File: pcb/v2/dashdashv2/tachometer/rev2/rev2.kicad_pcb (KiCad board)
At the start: 4 copper layers, 95 x 77 mm, 204 parts, among them J1 Tag connect, J2 RPM_CONN1, Q1 BSS138, Q2 BSS138, Q6 BSS138, Q7 BSS138, U1 W25Q128JVS, U2 LP5907MFX-3.3, U3 SRV05-4, U4 RP2040, U6 YAAJ_DCDC_StepDown_LM2596, Y1 12MHz

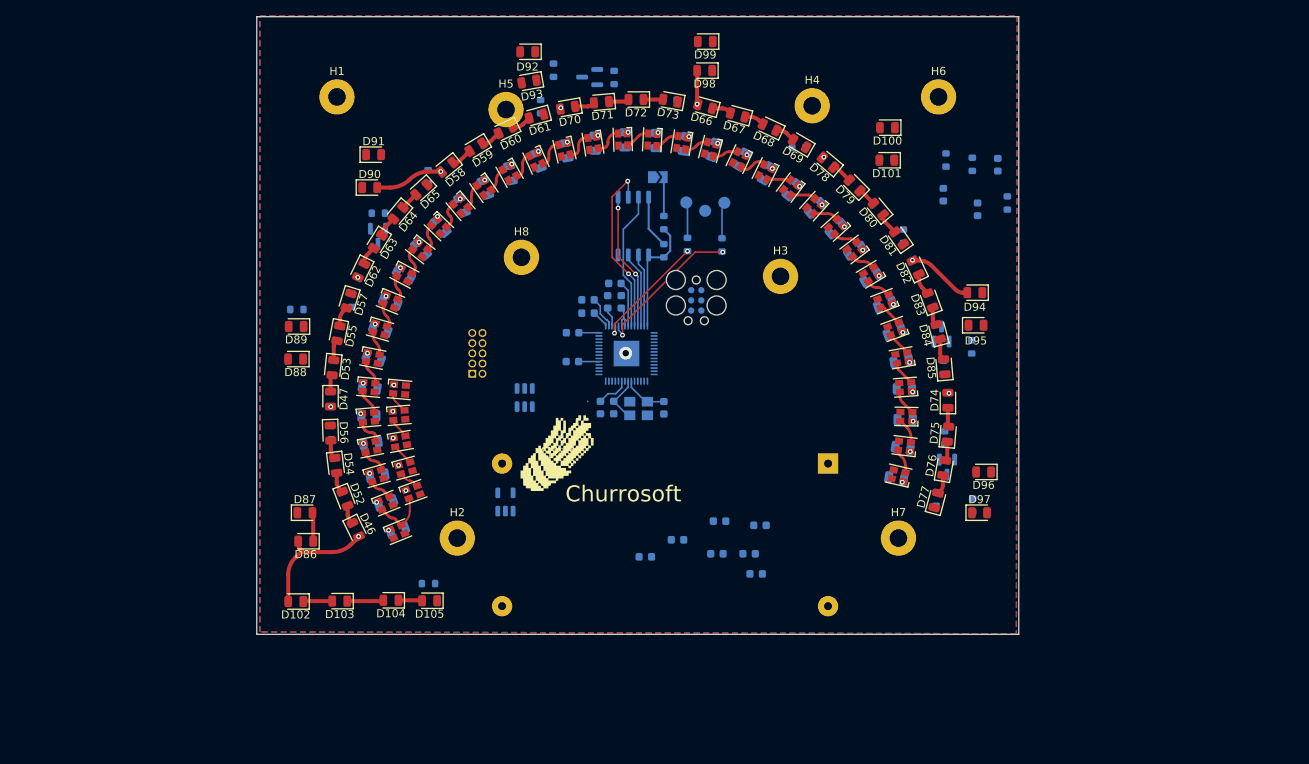
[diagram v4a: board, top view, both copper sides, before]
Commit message: routing backlight leds
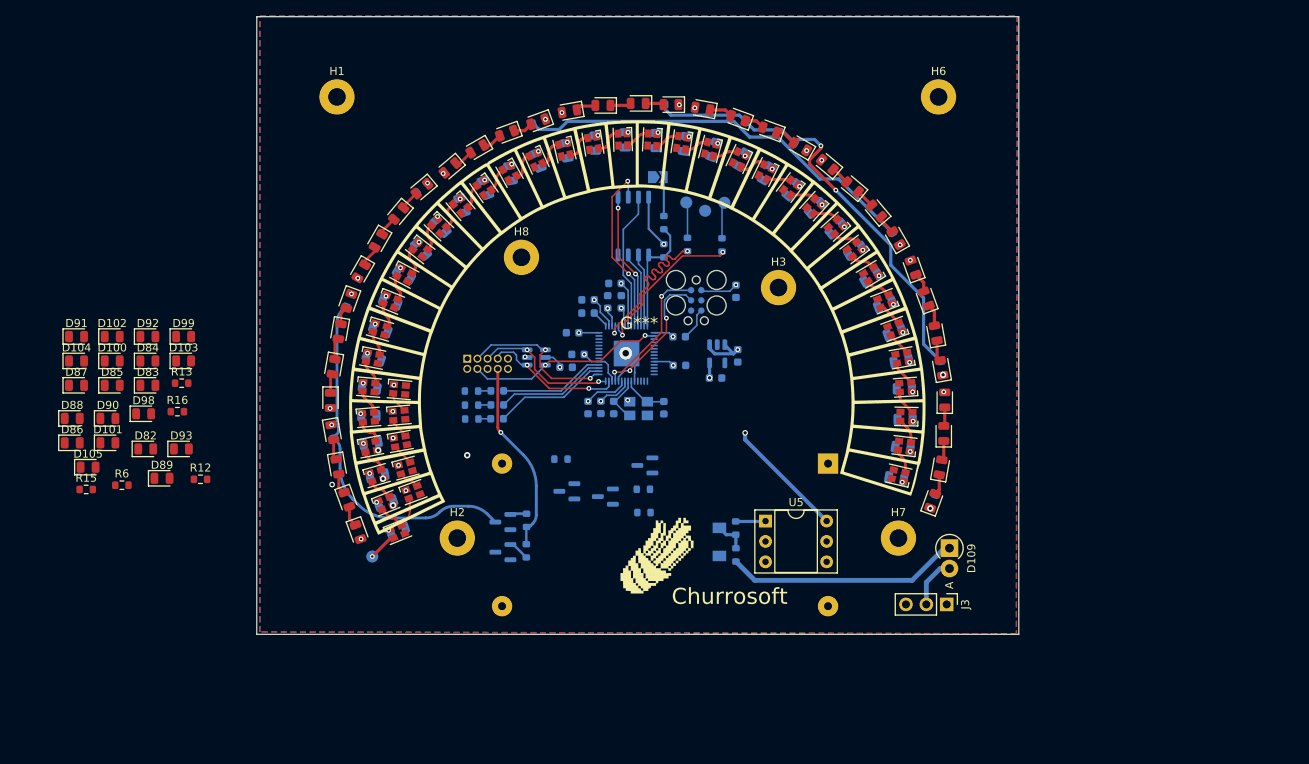
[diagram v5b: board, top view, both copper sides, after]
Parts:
- removed H5: MountingHole, MountingHole:MountingHole_2.2mm_M2_Pad
- removed R17, R19, R20: 1k 1/10W +-1%, Resistor_SMD:R_0603_1608Metric
- added D109: 1N4007, Diode_THT:D_DO-41_SOD81_P2.54mm_Vertical_AnodeUp, F.Cu at (186.4, 116.3)
- added D110: BZV55B5V1, Diode_SMD:D_MiniMELF, B.Cu at (157.7, 115.5)
- added G***: LOGO, LOGO, F.Cu at (147.7, 88.2)
- added J3: Conn_01x03, Connector_PinHeader_2.54mm:PinHeader_1x03_P2.54mm_Vertical, F.Cu at (186.0, 123.3)
- added Q8: BSS138, Package_TO_SOT_SMD:SOT-23, B.Cu at (148.4, 105.9)
- added R12: 1k 1/10W +-1%, Resistor_SMD:R_0603_1608Metric, F.Cu at (93.0, 107.7)
- added R13: 1k 1/10W +-1%, Resistor_SMD:R_0603_1608Metric, F.Cu at (90.6, 95.7)
- added R2: 1k 1/10W +-1%, Resistor_SMD:R_0603_1608Metric, B.Cu at (148.2, 108.9)
- added R36: 1k 1/10W +-1%, Resistor_SMD:R_0603_1608Metric, B.Cu at (159.7, 117.1)
- added R37: 330R 1/10W +-1%, Resistor_SMD:R_0603_1608Metric, B.Cu at (159.7, 113.8)
- added R6: 1k 1/10W +-1%, Resistor_SMD:R_0603_1608Metric, F.Cu at (83.2, 108.4)
- added U5: H11L1, Package_DIP:DIP-6_W7.62mm_Socket, F.Cu at (163.4, 112.9)
- H4: value MountingHole -> USB_GND; footprint MountingHole:MountingHole_2.2mm_M2_Pad -> TestPoint:TestPoint_Pad_D1.5mm; moved to B.Cu
- R15, R16: moved to F.Cu
- moved R15 108.0 mm to (78.7, 108.9), turned to 0 degrees
- moved D85 103.8 mm to (82.0, 96.0), turned to 0 degrees
- moved D101 103.3 mm to (81.4, 103.1), turned to 0 degrees
- moved D100 100.9 mm to (82.0, 92.9), turned to 0 degrees
- moved D82 98.6 mm to (86.2, 103.9), turned to 0 degrees
- moved D84 98.6 mm to (86.4, 92.9), turned to 0 degrees
- moved D83 98.1 mm to (86.4, 96.0), turned to 0 degrees
- moved D98 82.0 mm to (85.9, 99.5), turned to 0 degrees
- moved H4 78.5 mm to (114.4, 117.3), turned to 180 degrees
- moved R28 74.8 mm to (184.3, 110.4), turned to 70 degrees
- moved D99 74.7 mm to (90.9, 89.9), turned to 0 degrees
- moved D64 74.7 mm to (185.2, 106.2), turned to 80 degrees
- moved D65 74.6 mm to (184.3, 110.3), turned to 70 degrees
- moved D62 74.5 mm to (185.8, 97.8), turned to 90 degrees
- moved D63 74.5 mm to (185.6, 102.0), turned to 90 degrees
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- renumbered G*** to Churrosoft
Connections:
- H4 pad 1: (no net) -> /TACH_DIN
- R15 pad 1: Net-(D85-Pad1) -> Net-(D101-Pad1)
- R15 pad 2: /BA_3 -> /BA_5
- R16 pad 1: Net-(D89-Pad1) -> Net-(D105-Pad1)
- R16 pad 2: /BA_3 -> /BA_5
- U3 pad 1: CLK -> MOSI
- U3 pad 4: RPM_CS -> CLK
- U3 pad 6: MOSI -> RPM_CS
- U4 pad 27: CLK -> MOSI
- U4 pad 29: MOSI -> CLK
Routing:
- net +12LF: track 37.6 -> 108.9 mm, vias 9 -> 11
- net /BA_4: track 0.00 -> 56.6 mm, vias 0 -> 2
- net /BA_3: track 0.00 -> 51.4 mm
- net /BA_1: track 0.00 -> 44.6 mm
- net +3V3: track 19.2 -> 56.3 mm, vias 0 -> 12
- net Net-(D109-Pad1): track 0.00 -> 29.3 mm
- net RPM_CS: track 0.00 -> 24.8 mm, vias 0 -> 2
- net PWM_BACK_RPM: track 0.00 -> 24.2 mm, vias 0 -> 1
- net CLK: track 0.00 -> 20.0 mm, vias 0 -> 2
- net MISO: track 0.00 -> 18.0 mm, vias 0 -> 2
- net +1V1: track 12.5 -> 30.5 mm, vias 0 -> 3
- net /SYS_SWDIO: track 0.00 -> 17.6 mm, vias 0 -> 2
- net MOSI: track 0.00 -> 17.5 mm, vias 0 -> 2
- net /SYS_SWCLK: track 0.00 -> 16.9 mm, vias 0 -> 2
- net /LED_GREEN: track 0.00 -> 14.4 mm
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- added copper zone on In2.Cu, net +3V3
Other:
- board text removed: "Churrosoft"

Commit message: rpm routing v01
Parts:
- removed D102, D103, D104, D105: LED, LED_SMD:LED_0805_2012Metric
- removed R16: 1k 1/10W +-1%, Resistor_SMD:R_0603_1608Metric
- R12, R13, R15, R6: moved to B.Cu
- moved R15 111.0 mm to (189.7, 111.5)
- moved D100 109.9 mm to (191.0, 107.3)
- moved D101 108.7 mm to (189.8, 111.5)
- moved D98 104.8 mm to (189.7, 85.1)
- moved D99 98.9 mm to (189.8, 88.3)
- moved D92 96.0 mm to (178.7, 63.4)
- moved D93 95.2 mm to (178.8, 68.0)
- moved R13 92.3 mm to (178.7, 67.9)
- moved D91 85.9 mm to (155.7, 54.3)
- moved D90 85.9 mm to (155.7, 57.0)
- moved D88 70.6 mm to (133.9, 58.3)
- moved D89 69.3 mm to (134.0, 55.4)
- moved R12 66.3 mm to (133.9, 55.5)
- moved D86 51.4 mm to (114.4, 67.8)
- moved D87 44.1 mm to (114.2, 71.3)
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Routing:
- net /BA_5: track 0.00 -> 202.0 mm
- net /BA_2: track 0.00 -> 111.0 mm, vias 0 -> 3
- net /BA_3: track 51.4 -> 108.4 mm, vias 0 -> 2
- net /BA_4: track 56.6 -> 111.9 mm, vias 2 -> 4
- net +12LF: track 108.9 -> 139.8 mm, vias 11 -> 10
- net Net-(D87-Pad1): track 0.00 -> 30.7 mm
- net Net-(D91-Pad1): track 0.00 -> 29.5 mm
- net +5VA: track 7.47 -> 30.7 mm
- net Net-(D100-Pad2): track 0.00 -> 20.2 mm
- net Net-(D83-Pad1): track 0.00 -> 19.9 mm
- net PWM_BACK_RPM: track 24.2 -> 32.5 mm
- net Net-(D92-Pad1): track 0.00 -> 5.42 mm
- net Net-(D100-Pad1): track 0.00 -> 4.51 mm
- net Net-(D86-Pad1): track 0.00 -> 4.22 mm
- net Net-(Q8-Pad1): track 0.00 -> 4.11 mm
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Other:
- board text added: "DashDash RPM Counter v0.1"

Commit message: update neopixel
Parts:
- D1, D10, D11, D111, D112, D113, D114, D115, D12, D13, D14, D15, D16, D17, D18, D19, D2, D20, D21, D22, D23, D24, D25, D26, D27, D28, D29, D3, D30, D31, D32, D33, D34, D35, D36, D4, D5, D6, D7, D8, D9: footprint LED_SMD:LED_Cree-PLCC4_2x2mm_CW -> dashdash_lib:LED_WS2812-2020
- moved C47 0.41 mm to (180.1, 107.4), turned to 170 degrees
- moved C40 0.41 mm to (176.9, 82.2), turned to -150 degrees
- moved D113 0.40 mm to (118.3, 102.9)
- moved D111 0.39 mm to (119.9, 109.2)
- moved C46 0.38 mm to (180.9, 103.9), turned to 170 degrees
- moved C14 0.36 mm to (114.9, 106.9), turned to 20 degrees
- moved C18 0.36 mm to (114.5, 92.2), turned to -10 degrees
- moved D112 0.36 mm to (118.9, 106.2)
- moved C35 0.35 mm to (163.9, 69.6), turned to -120 degrees
- moved C42 0.35 mm to (179.8, 89.1), turned to -160 degrees
- moved C13 0.34 mm to (115.9, 110.3), turned to 20 degrees
- moved D114 0.33 mm to (118.1, 99.8)
- moved C21 0.32 mm to (118.4, 81.8), turned to -30 degrees
- moved C43 0.32 mm to (180.6, 92.8), turned to -170 degrees
- moved C12 0.32 mm to (117.3, 114.1), turned to 20 degrees
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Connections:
- D1 pad 1: +5VA -> Net-(D1-Pad1)
- D1 pad 2: Net-(D1-Pad2) -> GND
- D1 pad 3: GND -> /TACH_DIN
- D1 pad 4: /TACH_DIN -> +5VA
- D10 pad 1: +5VA -> Net-(D10-Pad1)
- D10 pad 2: Net-(D10-Pad2) -> GND
- D10 pad 3: GND -> Net-(D10-Pad3)
- D10 pad 4: Net-(D10-Pad4) -> +5VA
- D11 pad 1: +5VA -> Net-(D11-Pad1)
- D11 pad 2: Net-(D11-Pad2) -> GND
- D11 pad 3: GND -> Net-(D10-Pad1)
- D11 pad 4: Net-(D10-Pad2) -> +5VA
- D111 pad 1: +5VA -> Net-(D111-Pad1)
- D111 pad 2: Net-(D111-Pad2) -> GND
- D111 pad 3: GND -> Net-(D1-Pad1)
- D111 pad 4: Net-(D1-Pad2) -> +5VA
- D112 pad 1: +5VA -> Net-(D112-Pad1)
- D112 pad 2: Net-(D112-Pad2) -> GND
- D112 pad 3: GND -> Net-(D111-Pad1)
- D112 pad 4: Net-(D111-Pad2) -> +5VA
- D113 pad 1: +5VA -> Net-(D113-Pad1)
- D113 pad 2: Net-(D113-Pad2) -> GND
- D113 pad 3: GND -> Net-(D112-Pad1)
- D113 pad 4: Net-(D112-Pad2) -> +5VA
- D114 pad 1: +5VA -> Net-(D114-Pad1)
- D114 pad 2: Net-(D114-Pad2) -> GND
- D114 pad 3: GND -> Net-(D113-Pad1)
- D114 pad 4: Net-(D113-Pad2) -> +5VA
- D115 pad 1: +5VA -> unconnected-(D115-Pad1)
- D115 pad 2: unconnected-(D115-Pad2) -> GND
- D115 pad 3: GND -> Net-(D114-Pad1)
- D115 pad 4: Net-(D114-Pad2) -> +5VA
- D12 pad 1: +5VA -> Net-(D12-Pad1)
- D12 pad 2: Net-(D12-Pad2) -> GND
- D12 pad 3: GND -> Net-(D11-Pad1)
- D12 pad 4: Net-(D11-Pad2) -> +5VA
- D13 pad 1: +5VA -> Net-(D13-Pad1)
- D13 pad 2: Net-(D13-Pad2) -> GND
- D13 pad 3: GND -> Net-(D12-Pad1)
- D13 pad 4: Net-(D12-Pad2) -> +5VA
- D14 pad 1: +5VA -> Net-(D14-Pad1)
- D14 pad 2: Net-(D14-Pad2) -> GND
- D14 pad 3: GND -> Net-(D13-Pad1)
- D14 pad 4: Net-(D13-Pad2) -> +5VA
- D15 pad 1: +5VA -> Net-(D15-Pad1)
- D15 pad 2: Net-(D15-Pad2) -> GND
- D15 pad 3: GND -> Net-(D14-Pad1)
- D15 pad 4: Net-(D14-Pad2) -> +5VA
- D16 pad 1: +5VA -> Net-(D16-Pad1)
- D16 pad 2: Net-(D16-Pad2) -> GND
- D16 pad 3: GND -> Net-(D15-Pad1)
- D16 pad 4: Net-(D15-Pad2) -> +5VA
- D17 pad 1: +5VA -> Net-(D17-Pad1)
- D17 pad 2: Net-(D17-Pad2) -> GND
- D17 pad 3: GND -> Net-(D16-Pad1)
- D17 pad 4: Net-(D16-Pad2) -> +5VA
- D18 pad 1: +5VA -> Net-(D18-Pad1)
- D18 pad 2: Net-(D18-Pad2) -> GND
- D18 pad 3: GND -> Net-(D17-Pad1)
- D18 pad 4: Net-(D17-Pad2) -> +5VA
- D19 pad 1: +5VA -> Net-(D19-Pad1)
- D19 pad 2: Net-(D19-Pad2) -> GND
- D19 pad 3: GND -> Net-(D18-Pad1)
- D19 pad 4: Net-(D18-Pad2) -> +5VA
- D2 pad 1: +5VA -> Net-(D2-Pad1)
- D2 pad 2: Net-(D2-Pad2) -> GND
- D2 pad 3: GND -> Net-(D1-Pad1)
- D2 pad 4: Net-(D1-Pad2) -> +5VA
- D20 pad 1: +5VA -> Net-(D20-Pad1)
- D20 pad 2: Net-(D20-Pad2) -> GND
- D20 pad 3: GND -> Net-(D19-Pad1)
- D20 pad 4: Net-(D19-Pad2) -> +5VA
- D21 pad 1: +5VA -> Net-(D21-Pad1)
- D21 pad 2: Net-(D21-Pad2) -> GND
- D21 pad 3: GND -> Net-(D20-Pad1)
- D21 pad 4: Net-(D20-Pad2) -> +5VA
- D22 pad 1: +5VA -> Net-(D22-Pad1)
- D22 pad 2: Net-(D22-Pad2) -> GND
- D22 pad 3: GND -> Net-(D21-Pad1)
- D22 pad 4: Net-(D21-Pad2) -> +5VA
- D23 pad 1: +5VA -> Net-(D23-Pad1)
- D23 pad 2: Net-(D23-Pad2) -> GND
- D23 pad 3: GND -> Net-(D22-Pad1)
- D23 pad 4: Net-(D22-Pad2) -> +5VA
- D24 pad 1: +5VA -> Net-(D24-Pad1)
- D24 pad 2: Net-(D24-Pad2) -> GND
- D24 pad 3: GND -> Net-(D23-Pad1)
- D24 pad 4: Net-(D23-Pad2) -> +5VA
- D25 pad 1: +5VA -> Net-(D25-Pad1)
- D25 pad 2: Net-(D25-Pad2) -> GND
- D25 pad 3: GND -> Net-(D24-Pad1)
- D25 pad 4: Net-(D24-Pad2) -> +5VA
- D26 pad 1: +5VA -> Net-(D26-Pad1)
- D26 pad 2: Net-(D26-Pad2) -> GND
- D26 pad 3: GND -> Net-(D25-Pad1)
- D26 pad 4: Net-(D25-Pad2) -> +5VA
- D27 pad 1: +5VA -> Net-(D27-Pad1)
- D27 pad 2: Net-(D27-Pad2) -> GND
- D27 pad 3: GND -> Net-(D26-Pad1)
- D27 pad 4: Net-(D26-Pad2) -> +5VA
- D28 pad 1: +5VA -> Net-(D28-Pad1)
- D28 pad 2: Net-(D28-Pad2) -> GND
- D28 pad 3: GND -> Net-(D27-Pad1)
- D28 pad 4: Net-(D27-Pad2) -> +5VA
- D29 pad 1: +5VA -> Net-(D29-Pad1)
- D29 pad 2: Net-(D29-Pad2) -> GND
- D29 pad 3: GND -> Net-(D28-Pad1)
- D29 pad 4: Net-(D28-Pad2) -> +5VA
- D3 pad 1: +5VA -> Net-(D3-Pad1)
- D3 pad 2: Net-(D3-Pad2) -> GND
- D3 pad 3: GND -> Net-(D2-Pad1)
- D3 pad 4: Net-(D2-Pad2) -> +5VA
- D30 pad 1: +5VA -> Net-(D30-Pad1)
- D30 pad 2: Net-(D30-Pad2) -> GND
- D30 pad 3: GND -> Net-(D29-Pad1)
- D30 pad 4: Net-(D29-Pad2) -> +5VA
- D31 pad 1: +5VA -> Net-(D31-Pad1)
- D31 pad 2: Net-(D31-Pad2) -> GND
- D31 pad 3: GND -> Net-(D30-Pad1)
- D31 pad 4: Net-(D30-Pad2) -> +5VA
- D32 pad 1: +5VA -> Net-(D32-Pad1)
- D32 pad 2: Net-(D32-Pad2) -> GND
- D32 pad 3: GND -> Net-(D31-Pad1)
- D32 pad 4: Net-(D31-Pad2) -> +5VA
- D33 pad 1: +5VA -> Net-(D33-Pad1)
- D33 pad 2: Net-(D33-Pad2) -> GND
- D33 pad 3: GND -> Net-(D32-Pad1)
- D33 pad 4: Net-(D32-Pad2) -> +5VA
- D34 pad 1: +5VA -> Net-(D34-Pad1)
- D34 pad 2: Net-(D34-Pad2) -> GND
- D34 pad 3: GND -> Net-(D33-Pad1)
- D34 pad 4: Net-(D33-Pad2) -> +5VA
- D35 pad 1: +5VA -> Net-(D35-Pad1)
- D35 pad 2: Net-(D35-Pad2) -> GND
- D35 pad 3: GND -> Net-(D34-Pad1)
- D35 pad 4: Net-(D34-Pad2) -> +5VA
- D36 pad 1: +5VA -> Net-(D36-Pad1)
- D36 pad 2: Net-(D36-Pad2) -> GND
- D36 pad 3: GND -> Net-(D35-Pad1)
- D36 pad 4: Net-(D35-Pad2) -> +5VA
- D4 pad 1: +5VA -> Net-(D4-Pad1)
- D4 pad 2: Net-(D4-Pad2) -> GND
- D4 pad 3: GND -> Net-(D3-Pad1)
- D4 pad 4: Net-(D3-Pad2) -> +5VA
- D5 pad 1: +5VA -> Net-(D5-Pad1)
- D5 pad 2: Net-(D5-Pad2) -> GND
- D5 pad 3: GND -> Net-(D4-Pad1)
- D5 pad 4: Net-(D4-Pad2) -> +5VA
- D6 pad 1: +5VA -> Net-(D6-Pad1)
- D6 pad 2: Net-(D6-Pad2) -> GND
- D6 pad 3: GND -> Net-(D5-Pad1)
- D6 pad 4: Net-(D5-Pad2) -> +5VA
- D7 pad 1: +5VA -> Net-(D7-Pad1)
- D7 pad 2: Net-(D7-Pad2) -> GND
- D7 pad 3: GND -> Net-(D6-Pad1)
- D7 pad 4: Net-(D6-Pad2) -> +5VA
- D8 pad 1: +5VA -> Net-(D8-Pad1)
- D8 pad 2: Net-(D8-Pad2) -> GND
- D8 pad 3: GND -> Net-(D7-Pad1)
- D8 pad 4: Net-(D7-Pad2) -> +5VA
- D9 pad 1: +5VA -> Net-(D10-Pad3)
- D9 pad 2: Net-(D10-Pad4) -> GND
- D9 pad 3: GND -> Net-(D8-Pad1)
- D9 pad 4: Net-(D8-Pad2) -> +5VA
- U4 pad 14: unconnected-(U4-Pad14) -> /TACH_DIN
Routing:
- net /TACH_DIN: track 3.62 -> 53.6 mm, vias 1 -> 2
- net +5VA: track 30.7 -> 6.08 mm
- net Net-(D1-Pad1): track 0.00 -> 9.21 mm, vias 0 -> 2
- net Net-(D1-Pad2): track 6.95 -> 0.00 mm
- net Net-(D16-Pad2): track 3.64 -> 0.00 mm
- net Net-(D17-Pad2): track 3.60 -> 0.00 mm
- net Net-(D10-Pad3): track 0.00 -> 3.58 mm
- net Net-(D10-Pad2): track 3.57 -> 0.00 mm
- net Net-(D18-Pad2): track 3.56 -> 0.00 mm
- net Net-(D12-Pad2): track 3.56 -> 0.00 mm
- net Net-(D4-Pad1): track 0.00 -> 3.53 mm
- net Net-(D11-Pad2): track 3.50 -> 0.00 mm
- net Net-(D3-Pad1): track 0.00 -> 3.49 mm
- net Net-(D23-Pad2): track 3.49 -> 0.00 mm
- net Net-(D31-Pad1): track 0.00 -> 3.48 mm
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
